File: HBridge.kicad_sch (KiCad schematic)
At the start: 5 parts, among them J1 Conn_01x02_Pin, J2 Conn_01x03_Pin, U1 L298P

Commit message: h bridge hardware logic and fets
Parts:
- removed C1, C2: 100nF, Capacitor_SMD:C_0603_1608Metric, symbol Device:C_US
- removed J1: Conn_01x02_Pin, Connector:JWT_A3963_1x02_P3.96mm_Vertical, symbol Connector:Conn_01x02_Pin
- removed J2: Conn_01x03_Pin, Connector_PinHeader_2.54mm:PinHeader_1x03_P2.54mm_Horizontal, symbol Connector:Conn_01x03_Pin
- removed U1: L298P, Package_SO:HSOP-20-1EP_11.0x15.9mm_P1.27mm_SlugDown, symbol Driver_Motor:L298P
- added C3, C4, C5, C6, C7, C8, C9: C_US, Capacitor_SMD:C_0603_1608Metric, symbol Device:C_US
- added Motor Load: Conn_01x02_Pin, Connector:JWT_A3963_1x02_P3.96mm_Vertical, symbol Connector:Conn_01x02_Pin
- added Q1, Q2, Q3, Q4: DMG3402L, Package_TO_SOT_SMD:SOT-23, symbol Transistor_FET:DMG3402L
- added STM Input Enable: Conn_01x03_Pin, Connector_PinHeader_2.54mm:PinHeader_1x03_P2.54mm_Horizontal, symbol Connector:Conn_01x03_Pin
- added U2, U3, U4, U5: 74AHC1G08, Package_TO_SOT_SMD:SOT-23-5, symbol 74xGxx:74AHC1G08
- added U6, U7: 74LVC1GU04DRL, Package_TO_SOT_SMD:SOT-553, symbol 74xGxx:74LVC1GU04DRL
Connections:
- net +9V: now also C3.1, C4.1, C5.1, C6.1, C7.1, C8.1, C9.1, Q1.3 (D), Q3.2 (S), U2.5 (VCC), U3.5 (VCC), U4.3 (GND), U5.3 (GND), U6.5 (VCC), U7.3 (GND)
- net GND: now also C3.2, C4.2, C5.2, C6.2, C7.2, C8.2, C9.2, Q2.2 (S), Q4.3 (D), U2.3 (GND), U3.3 (GND), U4.5 (VCC), U5.5 (VCC), U6.3 (GND), U7.5 (VCC)
- new net: Q2.1 (G), U3.4
- new net: U3.1, U6.4
- new net: Q1.1 (G), U2.4
- new net: U5.2, U7.4
- new net: Q3.1 (G), U4.4
- new net: Q4.1 (G), U5.4
- new net Enable: STM Input Enable.1 (Pin_1), U2.2, U3.2, U4.1, U5.1
- new net Input1: STM Input Enable.3 (Pin_3), U2.1, U6.2
- new net Input2: STM Input Enable.2 (Pin_2), U4.2, U7.2
- new net MotorConnect1: Motor Load.2 (Pin_2), Q3.3 (D), Q4.2 (S)
- new net MotorConnect2: Motor Load.1 (Pin_1), Q1.2 (S), Q2.3 (D)
- no-connect marks 5 -> 0

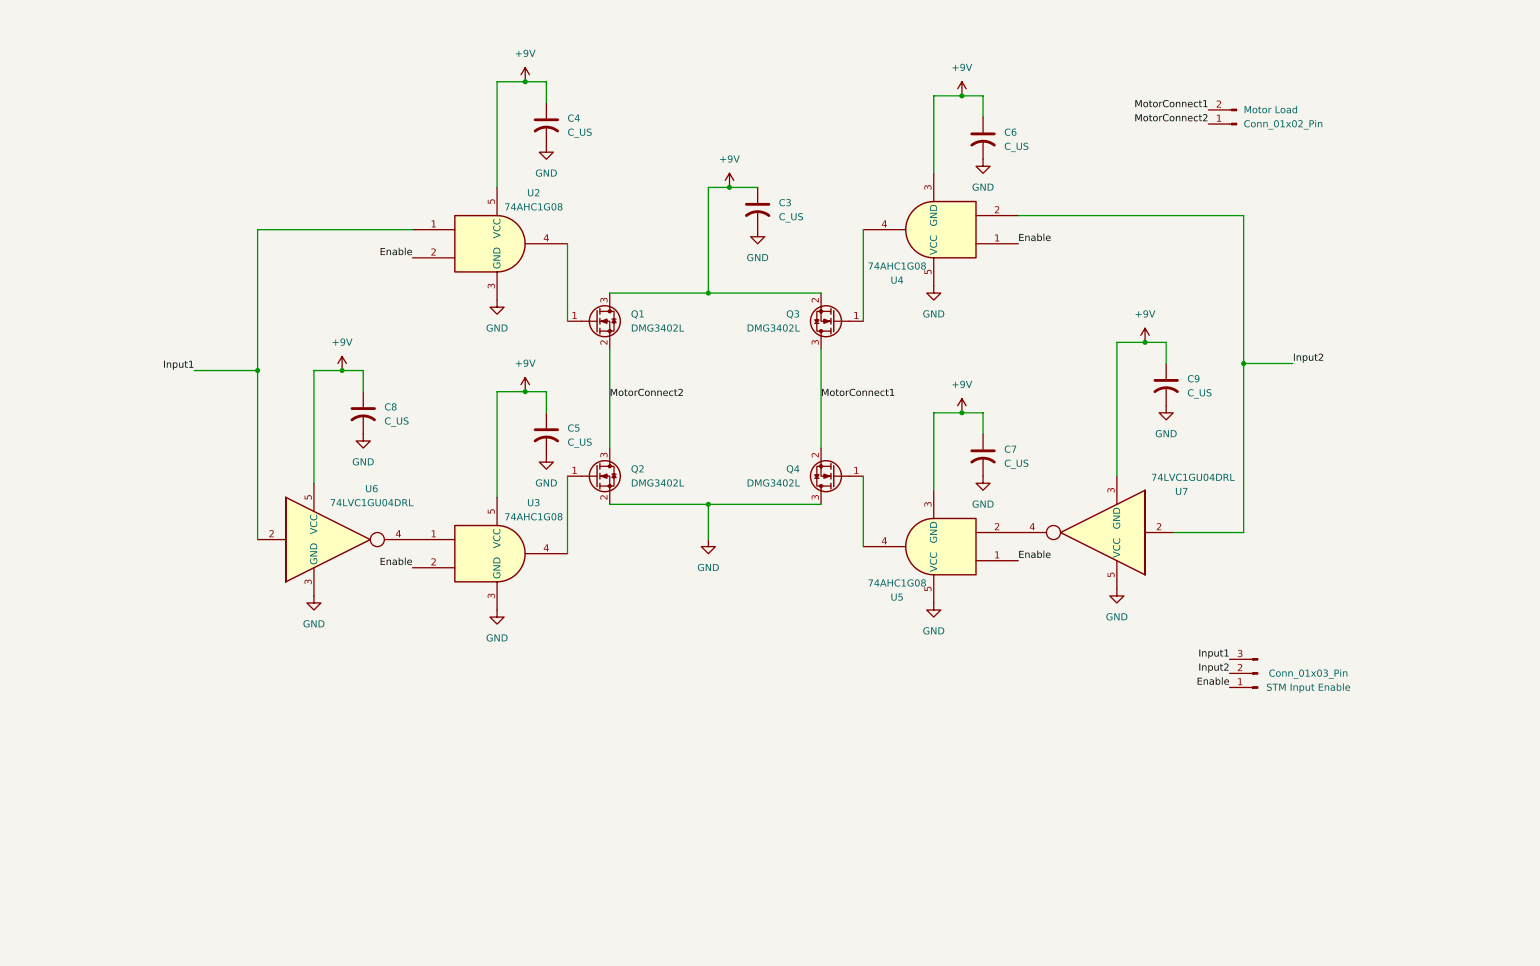
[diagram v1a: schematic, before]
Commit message: nmos and pmos hw logic schematic
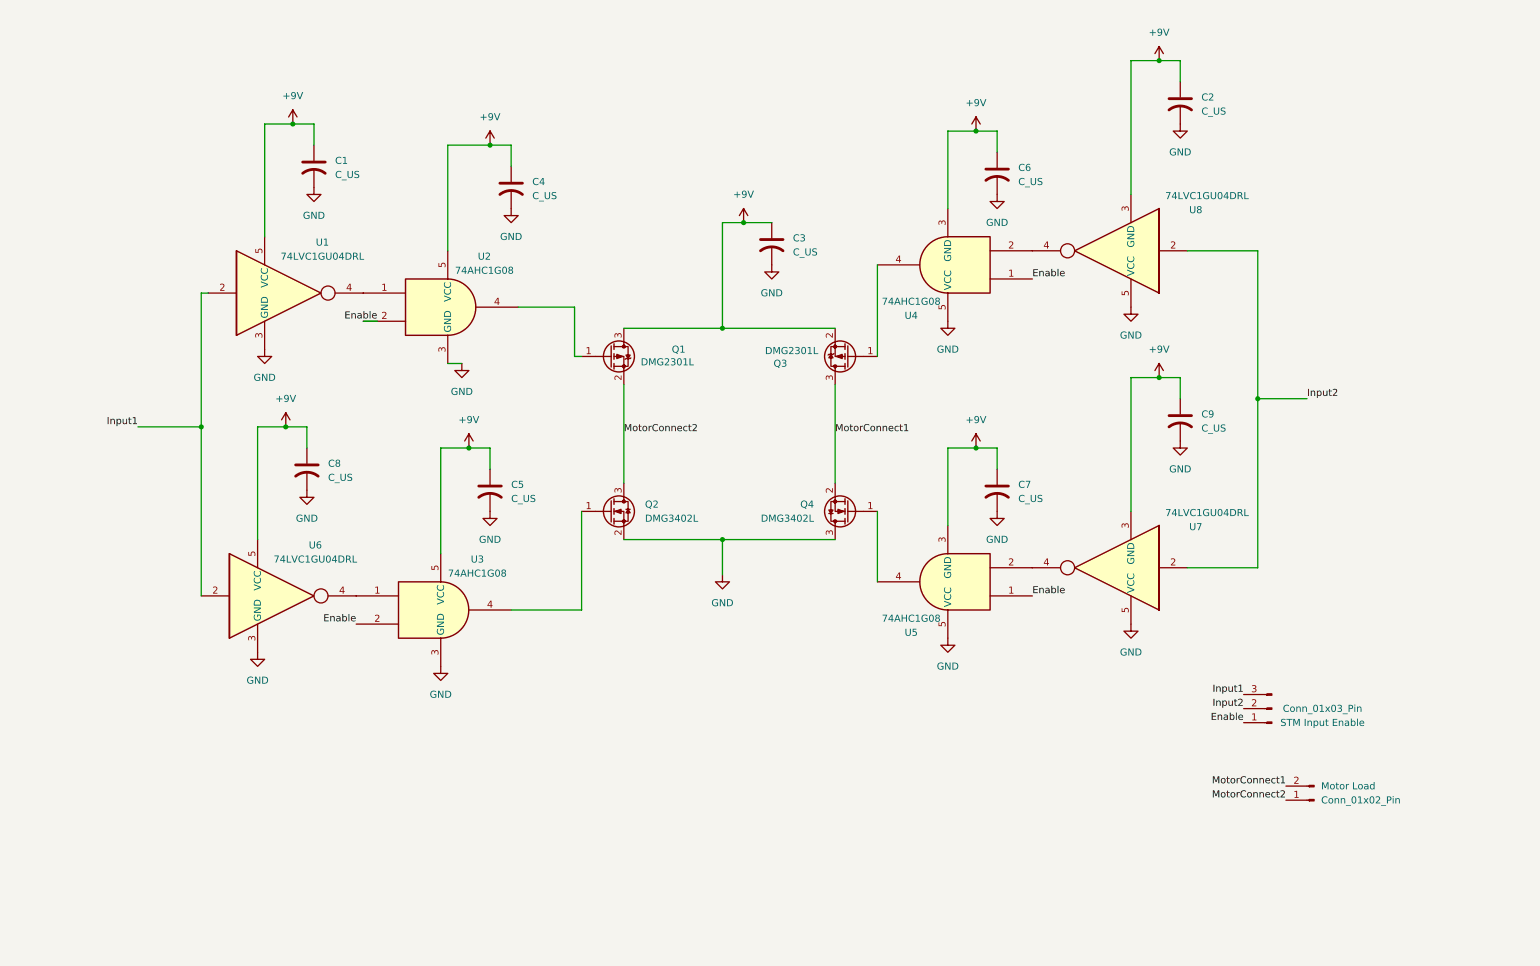
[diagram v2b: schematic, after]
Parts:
- removed Q1, Q3: DMG3402L, Package_TO_SOT_SMD:SOT-23, symbol Transistor_FET:DMG3402L
- added C1, C2: C_US, Capacitor_SMD:C_0603_1608Metric, symbol Device:C_US
- added Q1, Q3: DMG2301L, Package_TO_SOT_SMD:SOT-23, symbol Transistor_FET:DMG2301L
- added U1, U8: 74LVC1GU04DRL, Package_TO_SOT_SMD:SOT-553, symbol 74xGxx:74LVC1GU04DRL
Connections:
- net +9V: now also C1.1, C2.1, Q1.3 (D), Q3.2 (S), U1.5 (VCC), U8.3 (GND)
- net GND: now also C1.2, C2.2, U1.3 (GND), U8.5 (VCC)
- net Input1: now also U1.2; no longer U2.1
- net Input2: now also U8.2; no longer U4.2
- net MotorConnect1: now also Q3.3 (D)
- net MotorConnect2: now also Q1.2 (S)
- net at U2.4: now also Q1.1 (G)
- net at U4.4: now also Q3.1 (G)
- new net: U1.4, U2.1
- new net: U4.2, U8.4
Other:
- title: (none) -> H Bridge
- moved on the sheet: C3, C4, C5, C6, C7, C8, C9, Motor Load, Q2, Q4, STM Input Enable, U2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

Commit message: Add files via upload
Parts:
- removed Motor Load: Conn_01x02_Pin, Connector:JWT_A3963_1x02_P3.96mm_Vertical, symbol Connector:Conn_01x02_Pin
- removed STM Input Enable: Conn_01x03_Pin, Connector_PinHeader_2.54mm:PinHeader_1x03_P2.54mm_Horizontal, symbol Connector:Conn_01x03_Pin
- added 9VPower, MotorLoad: Conn_01x02_Pin, Connector_PinHeader_2.54mm:PinHeader_1x02_P2.54mm_Vertical, symbol Connector:Conn_01x02_Pin
- added C10: 10nF, Capacitor_SMD:C_0603_1608Metric, symbol Device:C_Small_US
- added C11: 0.01nF, Capacitor_SMD:C_0603_1608Metric, symbol Device:C_Small_US
- added C12: 1uF, Capacitor_SMD:C_0603_1608Metric, symbol Device:C_Small_US
- added STMInputEnable: Conn_01x03_Pin, Connector_PinHeader_2.54mm:PinHeader_1x03_P2.54mm_Vertical, symbol Connector:Conn_01x03_Pin
- added U10: LT1762, Package_SO:MSOP-8_3x3mm_P0.65mm, symbol Regulator_Linear:LT1762
- C1, C2, C3, C4, C5, C6, C7, C8, C9: value C_US -> 100nF
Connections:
- net +9V: now also Q1.2 (S), 9VPower.2 (Pin_2), C12.1, U10.5 (~{SHDN}), U10.8 (IN); no longer C1.1, C2.1, C4.1, C5.1, C6.1, C7.1, C8.1, C9.1, Q1.3 (D), U1.5 (VCC), U2.5 (VCC), U3.5 (VCC), U4.3 (GND), U5.3 (GND), U6.5 (VCC), U7.3 (GND), U8.3 (GND)
- net Enable: now also U4.2, U5.2; no longer U4.1, U5.1
- net GND: now also Q4.2 (S), U4.3 (GND), U5.3 (GND), U7.3 (GND), U8.3 (GND), 9VPower.1 (Pin_1), C10.2, C12.2, U10.4 (GND); no longer Q4.3 (D), U4.5 (VCC), U5.5 (VCC), U7.5 (VCC), U8.5 (VCC)
- net MotorConnect1: now also Q4.3 (D), MotorLoad.2 (Pin_2); no longer Q4.2 (S)
- net MotorConnect2: now also Q1.3 (D), MotorLoad.1 (Pin_1); no longer Q1.2 (S)
- net at U7.4: now also U5.1; no longer U5.2
- net at U8.4: now also U4.1; no longer U4.2
- new net: C11.1, U10.2 (ADJ)
- new net: C11.2, U10.3 (BYP)
- new net +3.3V: C1.1, C10.1, C2.1, C4.1, C5.1, C6.1, C7.1, C8.1, C9.1, U1.5 (VCC), U10.1 (OUT), U2.5 (VCC), U3.5 (VCC), U4.5 (VCC), U5.5 (VCC), U6.5 (VCC), U7.5 (VCC), U8.5 (VCC)
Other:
- moved on the sheet: C1, C2, C8, C9, Q4, U1, U4, U5, U6, U7, U8

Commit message: Add files via upload
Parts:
- 9VPower, MotorLoad: value Conn_01x02_Pin -> CONN HEADER VERT 2POS 2.54MM
- STMInputEnable: value Conn_01x03_Pin -> CONN HEADER VERT 3POS 2.54MM
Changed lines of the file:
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@@
 			)
 		)
-		(property "Value" "Conn_01x02_Pin"
+		(property "Value" "CONN HEADER VERT 2POS 2.54MM"
 			(at 203.2 151.1299 0)
 			(effects
@@
 			)
 		)
-		(property "Value" "Conn_01x02_Pin"
+		(property "Value" "CONN HEADER VERT 2POS 2.54MM"
 			(at 250.19 157.4799 0)
 			(effects
@@
 			)
 		)
-		(property "Value" "Conn_01x03_Pin"
+		(property "Value" "CONN HEADER VERT 3POS 2.54MM"
 			(at 242.57 140.9699 0)
 			(effects

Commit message: Add files via upload
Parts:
- renumbered 9VPower to 9VPower1, MotorLoad to MotorLoad1, STMInputEnable to STMInputEnable1
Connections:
- net Enable: now also STMInputEnable1.1 (Pin_1)
- net Input1: now also STMInputEnable1.3 (Pin_3)
- net Input2: now also STMInputEnable1.2 (Pin_2)
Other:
- note added: "H Bridge"
- note added: "LDO"
- note added: "Motor/STM Conns"
- moved on the sheet: C1, C10, C11, C12, C2, C3, C4, C5, C6, C7, C8, C9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

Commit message: Add files via upload
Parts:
- added R1: R_US, symbol Device:R_US
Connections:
- net +3.3V: now also R1.1
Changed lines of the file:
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@@
+	(symbol
+		(lib_id "power:+9V")
+		(at 266.7 21.59 0)
+		(unit 1)
+		(exclude_from_sim no)
+		(in_bom yes)
+		(on_board yes)
+		(dnp no)
+		(fields_autoplaced yes)
+		(property "Reference" "#PWR035"
+			(at 266.7 25.4 0)
+			(effects
+				(font
+					(size 1.27 1.27)
+				)
+				(hide yes)
+			)
+		)
+		(property "Value" "+3.3V"
+			(at 266.7 16.51 0)
+			(effects
+				(font
+					(size 1.27 1.27)
+				)
+			)
+		)
+		(property "Footprint" ""
+			(at 266.7 21.59 0)
+			(effects
+				(font
+					(size 1.27 1.27)
+				)
+				(hide yes)
+			)
+		)
+		(property "Datasheet" ""
+			(at 266.7 21.59 0)
+			(effects
+				(font
+					(size 1.27 1.27)
+				)
+				(hide yes)
+			)
+		)
+		(property "Description" "Power symbol creates a global label with name \"+9V\""
+			(at 266.7 21.59 0)
+			(effects
+				(font
+					(size 1.27 1.27)
+				)
+				(hide yes)
+			)
+		)
+		(pin "1"
+		)
+		(instances
+			(project "HBridge"
+				(path "/62656264-54cf-4073-b2a3-f26daf922ed7"
+					(reference "#PWR035")
+					(unit 1)
+				)
+			)
+		)
+	)
 	(symbol
 		(lib_id "power:+9V")
@@
 	)
 	(symbol
+		(lib_id "power:GND")
+		(at 266.7 35.56 0)
+		(unit 1)
+		(exclude_from_sim no)
+		(in_bom yes)
+		(on_board yes)
+		(dnp no)
+		(fields_autoplaced yes)
+		(property "Reference" "#PWR036"
+			(at 266.7 41.91 0)
+			(effects
+				(font
+					(size 1.27 1.27)
+				)
+				(hide yes)
+			)
+		)
+		(property "Value" "GND"
+			(at 266.7 40.64 0)
+			(effects
+				(font
+					(size 1.27 1.27)
+				)
+			)
+		)
+		(property "Footprint" ""
+			(at 266.7 35.56 0)
+			(effects
+				(font
+					(size 1.27 1.27)
+				)
+				(hide yes)
+			)
+		)
+		(property "Datasheet" ""
+			(at 266.7 35.56 0)
+			(effects
+				(font
+					(size 1.27 1.27)
+				)
+				(hide yes)
+			)
+		)
+		(property "Description" "Power symbol creates a global label with name \"GND\" , ground"
+			(at 266.7 35.56 0)
+			(effects
+				(font
+					(size 1.27 1.27)
+				)
+				(hide yes)
+			)
+		)
+		(pin "1"
+		)
+		(instances
+			(project ""
+				(path "/62656264-54cf-4073-b2a3-f26daf922ed7"
+					(reference "#PWR036")
+					(unit 1)
+				)
+			)
+		)
+	)
+	(symbol
 		(lib_id "74xGxx:74AHC1G08")
 		(at 170.18 109.22 0)
@@
 					(unit 1)
 				)
+			)
+		)
+	)
+	(symbol
+		(lib_id "Device:R_US")
+		(at 266.7 25.4 0)
+		(unit 1)
+		(exclude_from_sim no)
+		(in_bom yes)
+		(on_board yes)
+		(dnp no)
+		(fields_autoplaced yes)
+		(property "Reference" "R1"
+			(at 269.24 24.1299 0)
+			(effects
+				(font
+					(size 1.27 1.27)
+				)
+				(justify left)
+			)
+		)
+		(property "Value" "R_US"
+			(at 269.24 26.6699 0)
+			(effects
+				(font
+					(size 1.27 1.27)
+				)
+				(justify left)
+			)
+		)
+		(property "Footprint" ""
+			(at 267.716 25.654 90)
+			(effects
+				(font
+					(size 1.27 1.27)
+				)
+				(hide yes)
+			)
+		)
+		(property "Datasheet" "~"
+			(at 266.7 25.4 0)
+			(effects
+				(font
+					(size 1.27 1.27)
+				)
+				(hide yes)
+			)
+		)
+		(property "Description" "Resistor, US symbol"
+			(at 266.7 25.4 0)
+			(effects
+				(font
+					(size 1.27 1.27)
+				)
+				(hide yes)
+			)
+		)
+		(pin "1"
+		)
+		(pin "2"
+		)
+		(instances
+			(project ""
+				(path "/62656264-54cf-4073-b2a3-f26daf922ed7"
+					(reference "R1")
+					(unit 1)
+				)

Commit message: final revisions for layout
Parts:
- removed R1: R_US, symbol Device:R_US
- added H1: MountingHole, MountingHole:MountingHole_2.5mm, symbol Mechanical:MountingHole
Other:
- note added: "Mounting Holes"
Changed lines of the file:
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@@
 		)
 	)
+	(text "Mounting Holes"
+		(exclude_from_sim no)
+		(at 263.398 45.466 0)
+		(effects
+			(font
+				(size 1.27 1.27)
+			)
+		)
+	)
 	(text "H Bridge"
 		(exclude_from_sim no)
@@
 		)
 	)
+	(polyline
+		(pts
+			(xy 283.21 58.42) (xy 255.27 58.42)
+		)
+		(stroke
+			(width 0)
+			(type default)
+		)
+	)
 	(wire
 		(pts
@@
 		)
 	)
+	(polyline
+		(pts
+			(xy 255.27 43.18) (xy 283.21 43.18)
+		)
+		(stroke
+			(width 0)
+			(type default)
+		)
+	)
 	(wire
 		(pts
@@
 		)
 	)
+	(polyline
+		(pts
+			(xy 255.27 43.18) (xy 255.27 58.42)
+		)
+		(stroke
+			(width 0)
+			(type default)
+		)
+	)
 	(wire
 		(pts
@@
 		)
 	)
+	(polyline
+		(pts
+			(xy 283.21 43.18) (xy 283.21 58.42)
+		)
+		(stroke
+			(width 0)
+			(type default)
+		)
+	)
 	(wire
 		(pts
@@
 	(symbol
 		(lib_id "power:+9V")
-		(at 266.7 21.59 0)
-		(unit 1)
-		(exclude_from_sim no)
-		(in_bom yes)
-		(on_board yes)
-		(dnp no)
-		(fields_autoplaced yes)
-		(property "Reference" "#PWR035"
-			(at 266.7 25.4 0)
-			(effects
-				(font
-					(size 1.27 1.27)
-				)
-				(hide yes)
-			)
-		)
-		(property "Value" "+3.3V"
-			(at 266.7 16.51 0)
-			(effects
-				(font
-					(size 1.27 1.27)
-				)
-			)
-		)
-		(property "Footprint" ""
-			(at 266.7 21.59 0)
-			(effects
-				(font
-					(size 1.27 1.27)
-				)
-				(hide yes)
-			)
-		)
-		(property "Datasheet" ""
-			(at 266.7 21.59 0)
-			(effects
-				(font
-					(size 1.27 1.27)
-				)
-				(hide yes)
-			)
-		)
-		(property "Description" "Power symbol creates a global label with name \"+9V\""
-			(at 266.7 21.59 0)
-			(effects
-				(font
-					(size 1.27 1.27)
-				)
-				(hide yes)
-			)
-		)
-		(pin "1"
-		)
-		(instances
-			(project "HBridge"
-				(path "/62656264-54cf-4073-b2a3-f26daf922ed7"
-					(reference "#PWR035")
-					(unit 1)
-				)
-			)
-		)
-	)
-	(symbol
-		(lib_id "power:+9V")
 		(at 210.82 22.86 0)
 		(unit 1)
@@
 	)
 	(symbol
-		(lib_id "power:GND")
-		(at 266.7 35.56 0)
-		(unit 1)
-		(exclude_from_sim no)
-		(in_bom yes)
-		(on_board yes)
-		(dnp no)
-		(fields_autoplaced yes)
-		(property "Reference" "#PWR036"
-			(at 266.7 41.91 0)
-			(effects
-				(font
-					(size 1.27 1.27)
-				)
-				(hide yes)
-			)
-		)
-		(property "Value" "GND"
-			(at 266.7 40.64 0)
-			(effects
-				(font
-					(size 1.27 1.27)
-				)
-			)
-		)
-		(property "Footprint" ""
-			(at 266.7 35.56 0)
-			(effects
-				(font
-					(size 1.27 1.27)
-				)
-				(hide yes)
-			)
-		)
-		(property "Datasheet" ""
-			(at 266.7 35.56 0)
-			(effects
-				(font
-					(size 1.27 1.27)
-				)
-				(hide yes)
-			)
-		)
-		(property "Description" "Power symbol creates a global label with name \"GND\" , ground"
-			(at 266.7 35.56 0)
-			(effects
-				(font
-					(size 1.27 1.27)
-				)
-				(hide yes)
-			)
-		)
-		(pin "1"
-		)
-		(instances
-			(project ""
-				(path "/62656264-54cf-4073-b2a3-f26daf922ed7"
-					(reference "#PWR036")
-					(unit 1)
-				)
-			)
-		)
-	)
-	(symbol
 		(lib_id "74xGxx:74AHC1G08")
 		(at 170.18 109.22 0)
@@
 	)
 	(symbol
-		(lib_id "Device:R_US")
-		(at 266.7 25.4 0)
-		(unit 1)
-		(exclude_from_sim no)
-		(in_bom yes)
-		(on_board yes)
-		(dnp no)
-		(fields_autoplaced yes)
-		(property "Reference" "R1"
-			(at 269.24 24.1299 0)
-			(effects
-				(font
-					(size 1.27 1.27)
-				)
-				(justify left)
-			)
-		)
-		(property "Value" "R_US"
-			(at 269.24 26.6699 0)
-			(effects
-				(font
-					(size 1.27 1.27)
-				)
-				(justify left)
-			)
-		)
-		(property "Footprint" ""
-			(at 267.716 25.654 90)
-			(effects
-				(font
-					(size 1.27 1.27)
-				)
-				(hide yes)
-			)
-		)
-		(property "Datasheet" "~"
-			(at 266.7 25.4 0)
-			(effects
-				(font
-					(size 1.27 1.27)
-				)
-				(hide yes)
-			)
-		)
-		(property "Description" "Resistor, US symbol"
-			(at 266.7 25.4 0)
-			(effects
-				(font
-					(size 1.27 1.27)
-				)
-				(hide yes)
-			)
-		)
-		(pin "1"
-		)
-		(pin "2"
-		)
-		(instances
-			(project ""
-				(path "/62656264-54cf-4073-b2a3-f26daf922ed7"
-					(reference "R1")
-					(unit 1)
-				)
-			)
-		)
-	)
-	(symbol
 		(lib_id "74xGxx:74AHC1G08")
 		(at 80.01 59.69 0)
@@
 					(unit 1)
 				)
+			)
+		)
+	)
+	(symbol
+		(lib_id "Mechanical:MountingHole")
+		(at 264.16 52.07 0)
+		(unit 1)
+		(exclude_from_sim no)
+		(in_bom no)
+		(on_board yes)
+		(dnp no)
+		(fields_autoplaced yes)
+		(property "Reference" "H1"
+			(at 266.7 50.7999 0)
+			(effects
+				(font
+					(size 1.27 1.27)
+				)
+				(justify left)
+			)
+		)
+		(property "Value" "MountingHole"
+			(at 266.7 53.3399 0)
+			(effects
+				(font
+					(size 1.27 1.27)
+				)
+				(justify left)
+			)
+		)
+		(property "Footprint" "MountingHole:MountingHole_2.5mm"
+			(at 264.16 52.07 0)
+			(effects
+				(font
+					(size 1.27 1.27)
+				)
+				(hide yes)
+			)
+		)
+		(property "Datasheet" "~"
+			(at 264.16 52.07 0)
+			(effects
+				(font
+					(size 1.27 1.27)
+				)
+				(hide yes)
+			)
+		)
+		(property "Description" "Mounting Hole without connection"
+			(at 264.16 52.07 0)
+			(effects
+				(font
+					(size 1.27 1.27)
+				)
+				(hide yes)
+			)
+		)
+		(instances
+			(project ""
+				(path "/62656264-54cf-4073-b2a3-f26daf922ed7"
+					(reference "H1")
+					(unit 1)
+				)

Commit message: Add files via upload
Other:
- note added: "Power Connector"
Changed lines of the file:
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@@
+		)
+	)
+	(text "Power Connector"
+		(exclude_from_sim no)
+		(at 233.68 160.02 0)
+		(effects
+			(font
+				(size 1.27 1.27)
+			)
 		)
 	)
@@
 		(pts
 			(xy 129.54 44.45) (xy 134.62 44.45)
-		)
-		(stroke
-			(width 0)
-			(type default)
-		)
-	)
-	(wire
-		(pts
-			(xy 80.01 69.85) (xy 82.55 69.85)
 		)
 		(stroke
@@
 	(symbol
 		(lib_id "power:GND")
-		(at 82.55 69.85 0)
+		(at 80.01 69.85 0)
 		(unit 1)
 		(exclude_from_sim no)
@@
 		(fields_autoplaced yes)
 		(property "Reference" "#PWR013"
-			(at 82.55 76.2 0)
+			(at 80.01 76.2 0)
 			(effects
 				(font
@@
 		)
 		(property "Value" "GND"
-			(at 82.55 74.93 0)
+			(at 80.01 74.93 0)
 			(effects
 				(font
@@
 		)
 		(property "Footprint" ""
-			(at 82.55 69.85 0)
+			(at 80.01 69.85 0)
 			(effects
 				(font
@@
 		)
 		(property "Datasheet" ""
-			(at 82.55 69.85 0)
+			(at 80.01 69.85 0)
 			(effects
 				(font
@@
 		)
 		(property "Description" "Power symbol creates a global label with name \"GND\" , ground"
-			(at 82.55 69.85 0)
-			(effects
-				(font
+			(at 80.01 69.85 0)
+			(effects
+				(font
